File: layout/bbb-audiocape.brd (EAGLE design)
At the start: 69.2 x 54.6 mm, 42 parts, among them U1 TLV320AIC3104, U2 V_REG_LDOSMD

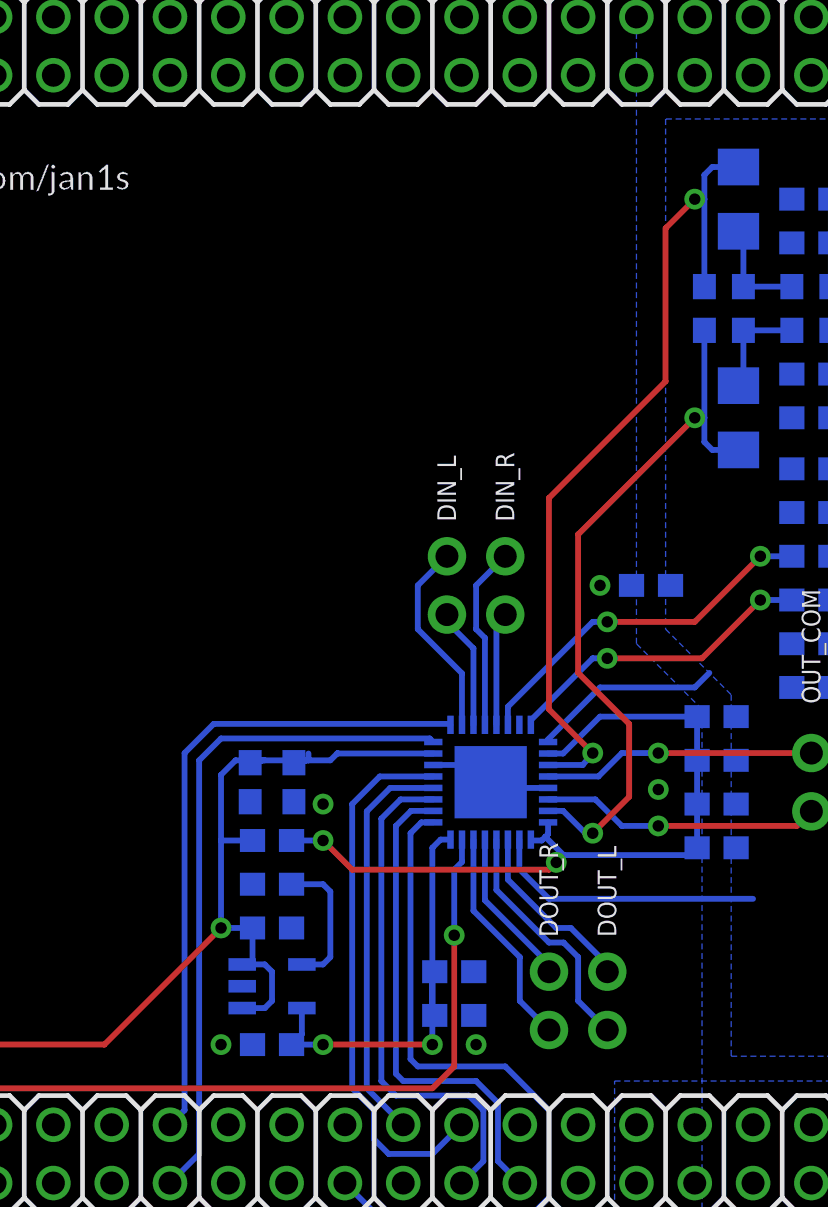
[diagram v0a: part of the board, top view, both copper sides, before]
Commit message: Added some vias
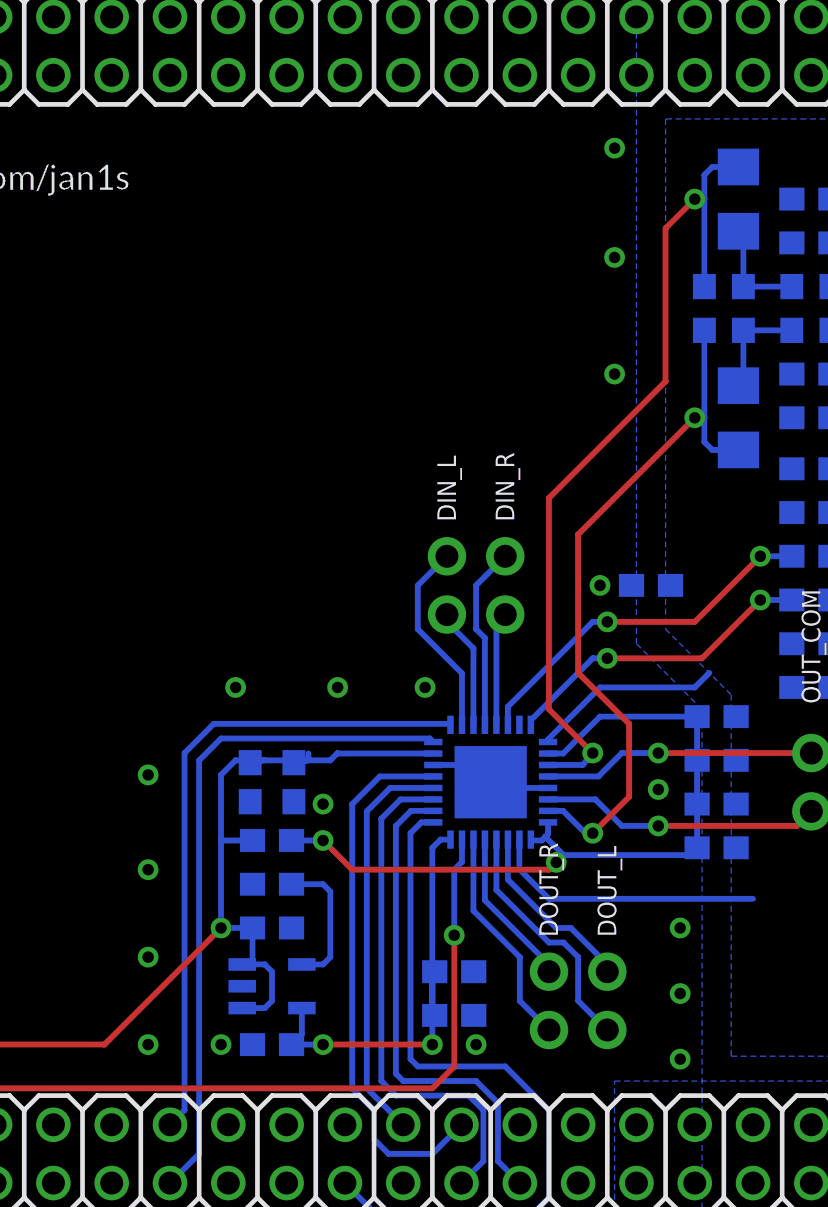
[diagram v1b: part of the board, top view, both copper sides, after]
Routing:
- net DGND: vias 5 -> 18
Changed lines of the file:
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@@
 <via x="56.515" y="9.2075" extent="1-16" drill="0.5"/>
 <via x="61.9125" y="29.21" extent="1-16" drill="0.5"/>
+<via x="54.2925" y="24.765" extent="1-16" drill="0.5"/>
+<via x="65.405" y="14.2875" extent="1-16" drill="0.5"/>
+<via x="65.405" y="8.5725" extent="1-16" drill="0.5"/>
+<via x="65.405" y="11.43" extent="1-16" drill="0.5"/>
+<via x="62.5475" y="38.4175" extent="1-16" drill="0.5"/>
+<via x="62.5475" y="48.26" extent="1-16" drill="0.5"/>
+<via x="62.5475" y="43.4975" extent="1-16" drill="0.5"/>
+<via x="50.4825" y="24.765" extent="1-16" drill="0.5"/>
+<via x="46.0375" y="24.765" extent="1-16" drill="0.5"/>
+<via x="42.2275" y="20.955" extent="1-16" drill="0.5"/>
+<via x="42.2275" y="16.8275" extent="1-16" drill="0.5"/>
+<via x="42.2275" y="13.0175" extent="1-16" drill="0.5"/>
+<via x="42.2275" y="9.2075" extent="1-16" drill="0.5"/>
 </signal>
 <signal name="SCL">
